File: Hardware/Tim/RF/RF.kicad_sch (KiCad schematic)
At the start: 15 parts, among them J4 U.FL, U8 DRF1262TL, Y2 32.768k

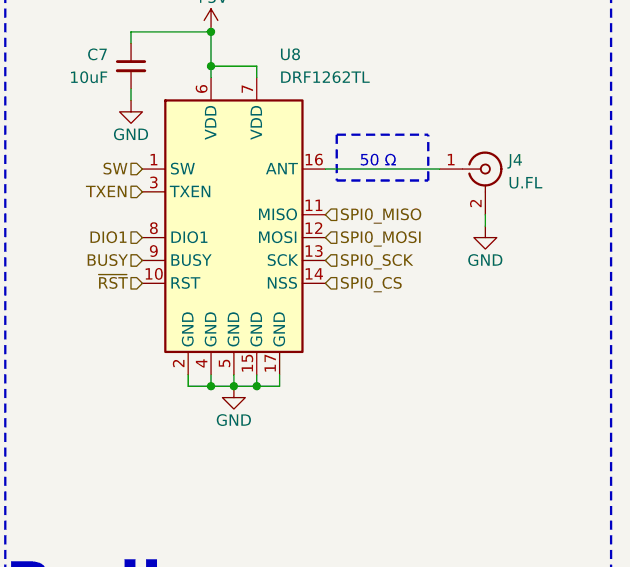
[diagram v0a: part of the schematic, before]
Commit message: Added color sensors disconnected GPIO in muxing crisis
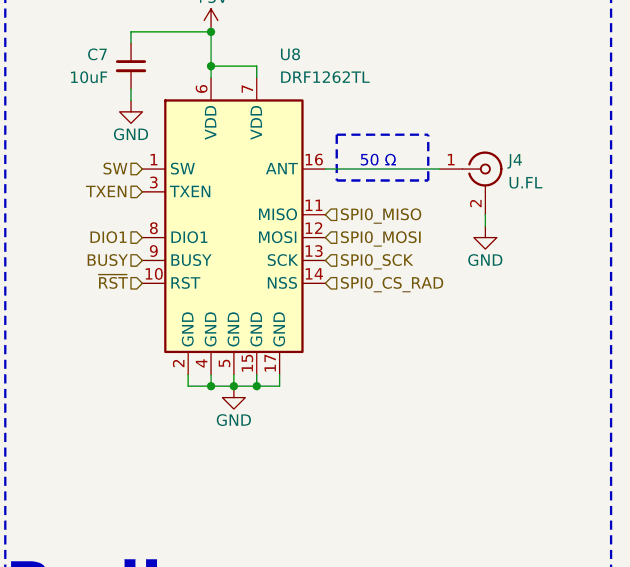
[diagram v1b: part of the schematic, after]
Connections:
- net SPI0_CS renamed SPI0_CS_RAD
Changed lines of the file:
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@@
     (effects (font (size 1.27 1.27)) (justify left))
   )
-  (hierarchical_label "SPI0_CS" (shape input) (at 209.55 95.25 0) (fields_autoplaced)
+  (hierarchical_label "SPI0_CS_RAD" (shape input) (at 209.55 95.25 0) (fields_autoplaced)
     (effects (font (size 1.27 1.27)) (justify left))
   )

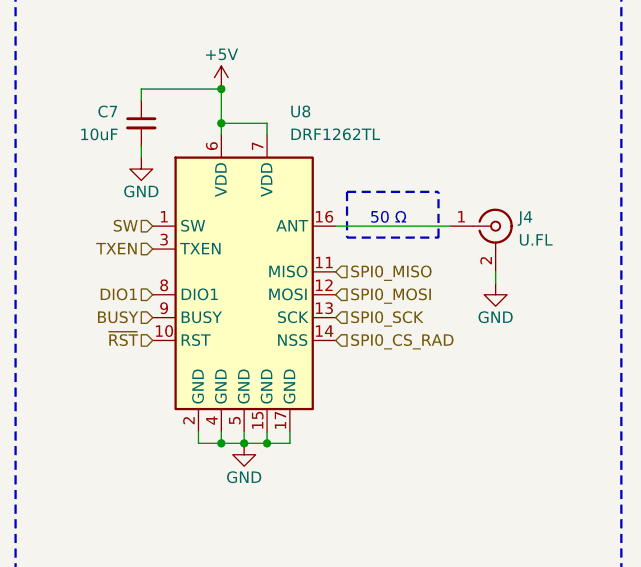
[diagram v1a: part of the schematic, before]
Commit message: Made it all one board due to large space allowed
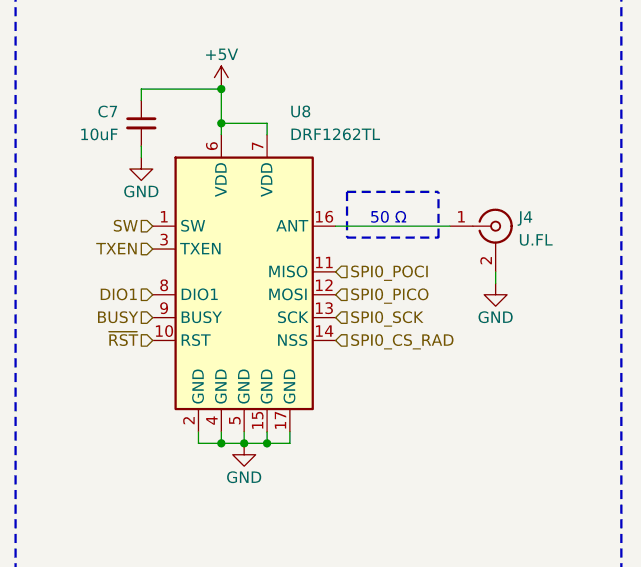
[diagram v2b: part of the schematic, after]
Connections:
- net SPI0_MISO renamed SPI0_POCI
- net SPI0_MOSI renamed SPI0_PICO
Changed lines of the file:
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@@
     (effects (font (size 1.27 1.27)) (justify left))
   )
-  (hierarchical_label "SPI0_MOSI" (shape input) (at 209.55 90.17 0) (fields_autoplaced)
+  (hierarchical_label "SPI0_PICO" (shape input) (at 209.55 90.17 0) (fields_autoplaced)
     (effects (font (size 1.27 1.27)) (justify left))
   )
-  (hierarchical_label "SPI0_MISO" (shape input) (at 209.55 87.63 0) (fields_autoplaced)
+  (hierarchical_label "SPI0_POCI" (shape input) (at 209.55 87.63 0) (fields_autoplaced)
     (effects (font (size 1.27 1.27)) (justify left))
   )
